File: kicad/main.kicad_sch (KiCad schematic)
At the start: 15 parts, among them J1 Barrel_Jack, J2 Conn, J3 VIA1, J4 VIA2, U1 DS1813-5+, U2 W65C816SxP, U3 L7805, U4 ATF16V8, U5 AS6C4008-55PCN, U6 27C512, U7 74LS573, U8 W65C22NxP, U9 74HC245, X1 CXO_DIP14

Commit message: v0.1 PCB
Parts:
- added C1: 0.1uF, Capacitor_THT:C_Disc_D3.0mm_W1.6mm_P2.50mm, symbol Device:C
- added C2, C3, C4: 0.1uF, my:C_Disc_VeryLong, symbol Device:C
- added C5, C6, C7: 0.1uF, my:C_Disc_Long, symbol Device:C
- added C8: 10uF, Capacitor_THT:CP_Radial_D6.3mm_P2.50mm, symbol Device:C_Polarized
- added U10: 74HC14, Package_DIP:DIP-14_W7.62mm_Socket, symbol 74xx:74HC14
- U6: footprint Package_DIP:DIP-28_W15.24mm_Socket -> my:ZIF28
- U7: value 74LS573 -> 74HC573
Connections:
- net +5V: now also C1.1, C2.1, C3.1, C4.1, C5.1, C6.1, C7.1, C8.1, U10.14 (VCC); no longer U8.24 (CS1)
- net CLK: now also U10.2; no longer U4.14 (IO6)
- net GND: now also C1.2, C2.2, C3.2, C4.2, C5.2, C6.2, C7.2, C8.2, U10.11, U10.13, U10.5, U10.7 (GND), U10.9
- net ~{CLK}: now also U10.4; no longer U4.13 (IO7)
- net VDA: now reaches U2.39 (VDA)
- net VDA: now also U8.24 (CS1)
- new net: U10.1, U4.14 (IO6)
- new net: U10.3, U4.13 (IO7)
- no-connect marks 9 -> 12
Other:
- note added: "Address Decoder"
- note added: "Address Demux"
- note added: "CPU"
- note added: "I/O"
- note added: "Power/Reset"
- note added: "RAM/ROM"
- moved on the sheet: J1, J2, J3, J4, RN1, U1, U2, U3, U4, U5, U6, U7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

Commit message: v0.1 final PCB
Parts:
- removed J2: Conn, Connector_PinHeader_2.54mm:PinHeader_1x05_P2.54mm_Vertical, symbol Connector:Conn_01x05_Pin
- removed J4: VIA2, Connector_PinHeader_2.54mm:PinHeader_1x12_P2.54mm_Vertical, symbol Connector:Conn_01x12_Pin
- removed U7: 74HC573, Package_DIP:DIP-20_W7.62mm_Socket, symbol 74xx:74LS573
- added H1, H2: MountingHole_Pad, MountingHole:MountingHole_2.5mm_Pad, symbol Mechanical:MountingHole_Pad
- added LCD1: ~, my:2004A-OLED, symbol lcd:2004A-OLED
- added U6: 74HC273, Package_DIP:DIP-20_W7.62mm_Socket, symbol 74xx:74HC273
- renumbered U2 to U1, U5 to U2, U6 to U3, U8 to U4, U4 to U5, U9 to U7, U3 to U8, U1 to U9
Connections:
- net +5V: now also LCD1.2 (Vdd), U6.20 (VCC)
- net A_{0}: now also LCD1.4 (RS)
- net A_{16}: now also U6.2 (Q0)
- net A_{17}: now also U6.5 (Q1)
- net A_{18}: now also U6.6 (Q2)
- net A_{19}: now also U6.9 (Q3)
- net A_{20}: now also U6.12 (Q4)
- net A_{21}: now also U6.15 (Q5)
- net A_{22}: now also U6.16 (Q6)
- net A_{23}: now also U6.19 (Q7)
- net CLK: now also U6.11 (Cp)
- net DB_{0}: now also U6.3 (D0)
- net DB_{1}: now also U6.4 (D1)
- net DB_{2}: now also U6.7 (D2)
- net DB_{3}: now also U6.8 (D3)
- net DB_{4}: now also U6.13 (D4)
- net DB_{5}: now also U6.14 (D5)
- net DB_{6}: now also U6.17 (D6)
- net DB_{7}: now also U6.18 (D7)
- net D_{0}: now also LCD1.7 (D_{0})
- net D_{1}: now also LCD1.8 (D_{1})
- net D_{2}: now also LCD1.9 (D_{2})
- net D_{3}: now also LCD1.10 (D_{3})
- net D_{4}: now also LCD1.11 (D_{4})
- net D_{5}: now also LCD1.12 (D_{5})
- net D_{6}: now also LCD1.13 (D_{6})
- net D_{7}: now also LCD1.14 (D_{7})
- net GND: now also LCD1.1 (GND), U6.10 (GND)
- net R~{W}: now also LCD1.5 (R~{W})
- net ~{RD}: now also U5.15 (IO5); no longer U5.16 (IO4)
- net ~{RES}: now also U6.1 (~{Mr})
- net ~{WD}: now also U5.14 (IO6); no longer U5.15 (IO5)
- net at U10.1: now also U5.13 (IO7); no longer U5.14 (IO6)
- net at U5.12 (IO8): now also U10.3
- new net LCDEN: LCD1.6 (E), U5.16 (IO4)
- no-connect marks 12 -> 28
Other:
- note added: "20x04 OLED"
- moved on the sheet: C1, C2, C3, C4, C5, C6, C7, J3, U10A

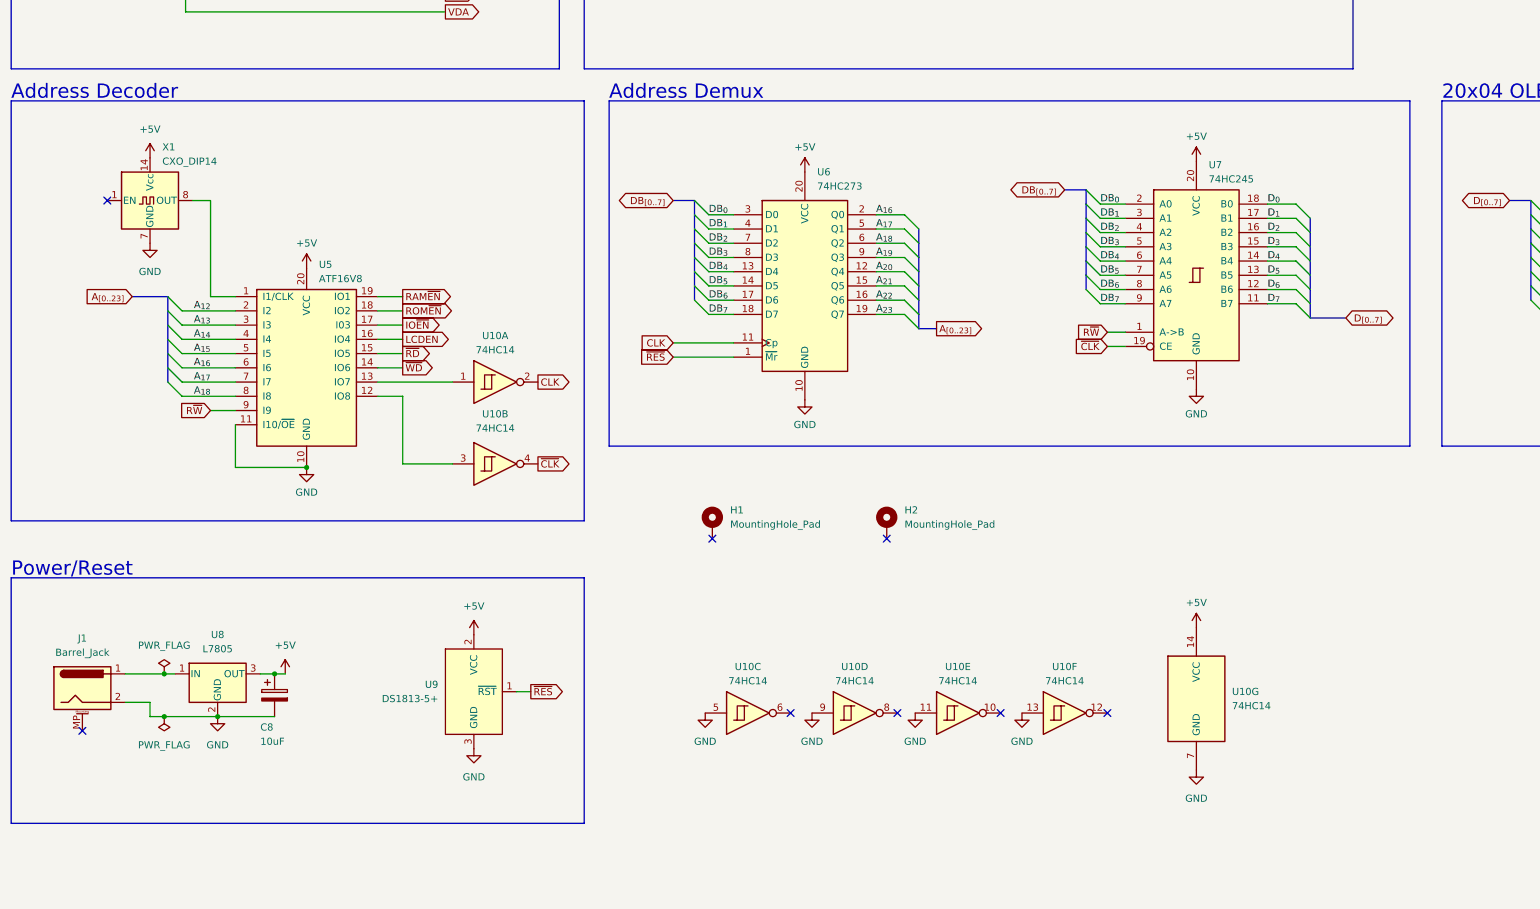
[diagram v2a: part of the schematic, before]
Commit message: Add 74HC00 for R/W qualification to save ATF pins for slow mode
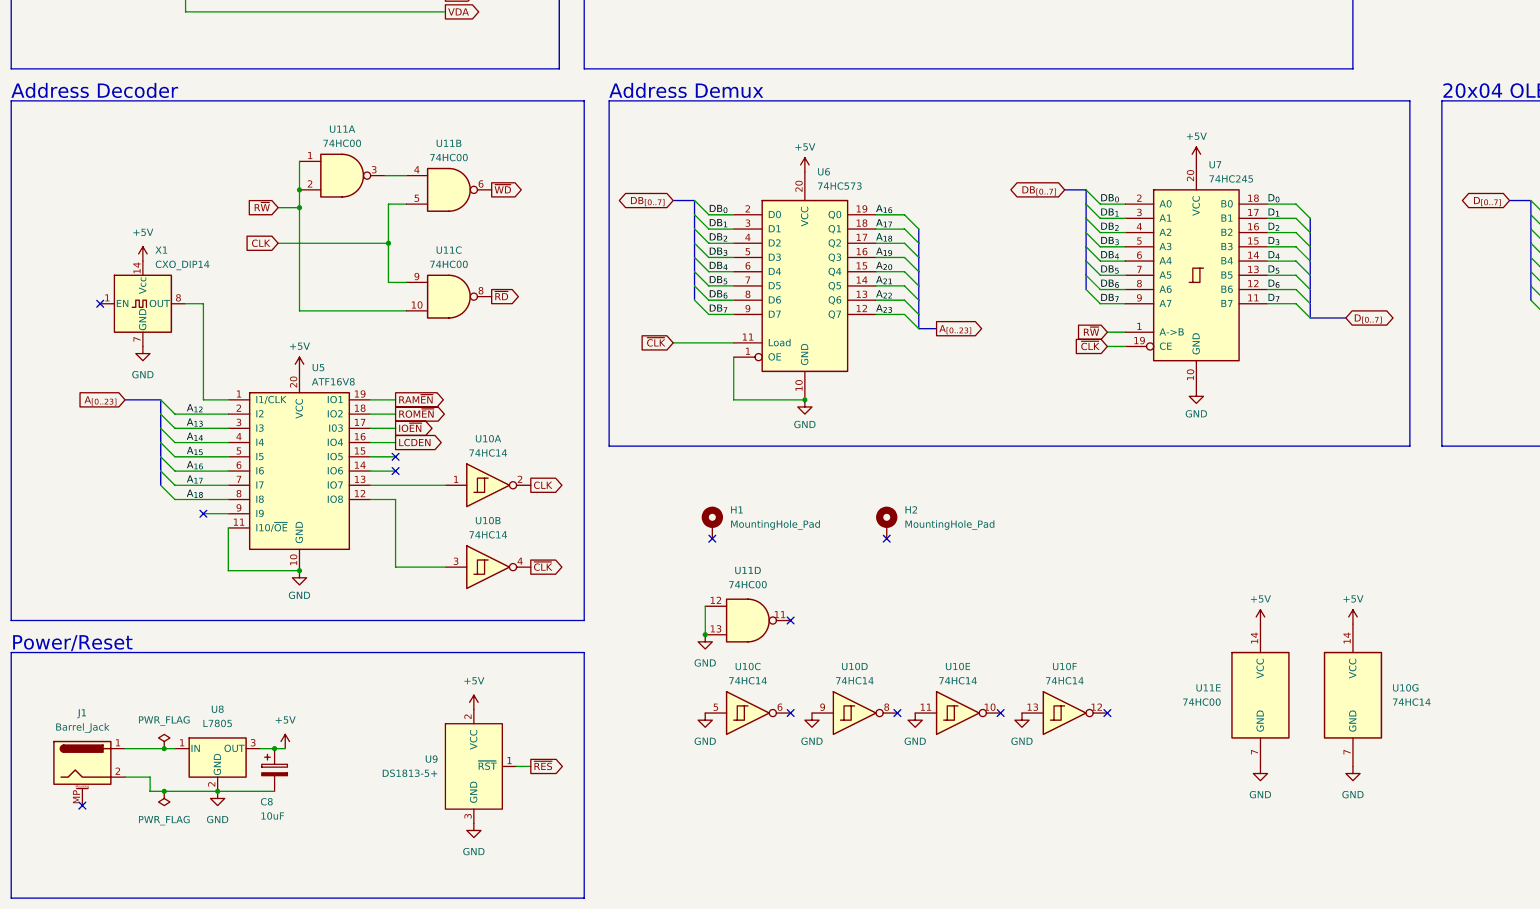
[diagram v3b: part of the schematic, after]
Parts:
- removed U6: 74HC273, Package_DIP:DIP-20_W7.62mm_Socket, symbol 74xx:74HC273
- added U11: 74HC00, Package_DIP:DIP-14_W7.62mm_Socket, symbol 74xx:74HC00
- added U6: 74HC573, Package_DIP:DIP-20_W7.62mm_Socket, symbol 74xx:74LS573
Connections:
- net +5V: now also U11.14 (VCC), U6.20 (VCC)
- net A_{16}: now also U6.19 (Q0)
- net A_{17}: now also U6.18 (Q1)
- net A_{18}: now also U6.17 (Q2)
- net A_{19}: now also U6.16 (Q3)
- net A_{20}: now also U6.15 (Q4)
- net A_{21}: now also U6.14 (Q5)
- net A_{22}: now also U6.13 (Q6)
- net A_{23}: now also U6.12 (Q7)
- net CLK: now also U11.5, U11.9
- net DB_{0}: now also U6.2 (D0)
- net DB_{1}: now also U6.3 (D1)
- net DB_{2}: now also U6.4 (D2)
- net DB_{3}: now also U6.5 (D3)
- net DB_{4}: now also U6.6 (D4)
- net DB_{5}: now also U6.7 (D5)
- net DB_{6}: now also U6.8 (D6)
- net DB_{7}: now also U6.9 (D7)
- net GND: now also U11.12, U11.13, U11.7 (GND), U6.1 (OE), U6.10 (GND)
- net R~{W}: now also U11.1, U11.10, U11.2; no longer U5.9 (I9)
- net ~{CLK}: now also U6.11 (Load)
- net ~{RD}: now also U11.8; no longer U5.15 (IO5)
- net ~{WD}: now also U11.6; no longer U5.14 (IO6)
- new net: U11.3, U11.4
- no-connect marks 28 -> 32
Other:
- moved on the sheet: C8, J1, U10G, U5, U8, U9, X1
